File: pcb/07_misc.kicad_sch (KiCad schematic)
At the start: 0 parts

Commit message: Added four mounting holes connected to chassis with decoupling to gnd and one single connection from chassis to gnd
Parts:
- added C701, C702, C703, C704: 1nF 1kV, FluxNode-FOC:C_0603_1608_DensityHigh, symbol Device:C
- added H701, H702, H703, H704: MountingHole_Pad, MountingHole:MountingHole_3.2mm_M3_Pad_Via, symbol Mechanical:MountingHole_Pad
- added R701, R702, R703, R704: 0R, FluxNode-FOC:R_0603_1608_DensityHigh, symbol Device:R
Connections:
- new net CHASSIS: C701.1, C702.1, C703.1, C704.1, H701.1, H702.1, H703.1, H704.1, R701.1, R702.1, R703.1, R704.1
- new net GND: C701.2, C702.2, C703.2, C704.2, R701.2, R702.2, R703.2, R704.2

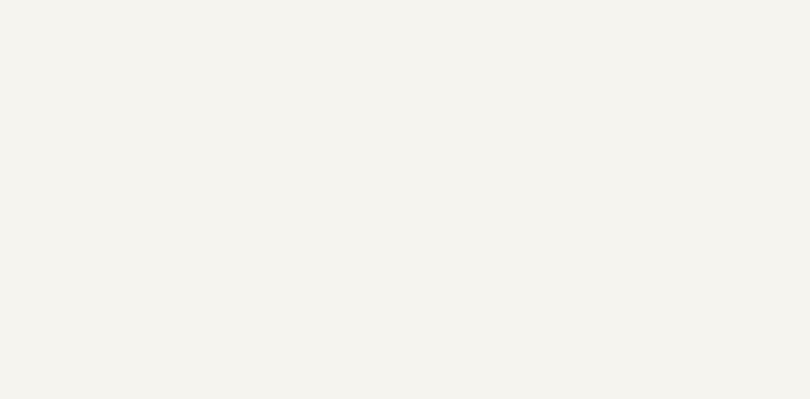
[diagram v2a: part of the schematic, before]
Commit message: Added fiducials for the top and bottom PCB side
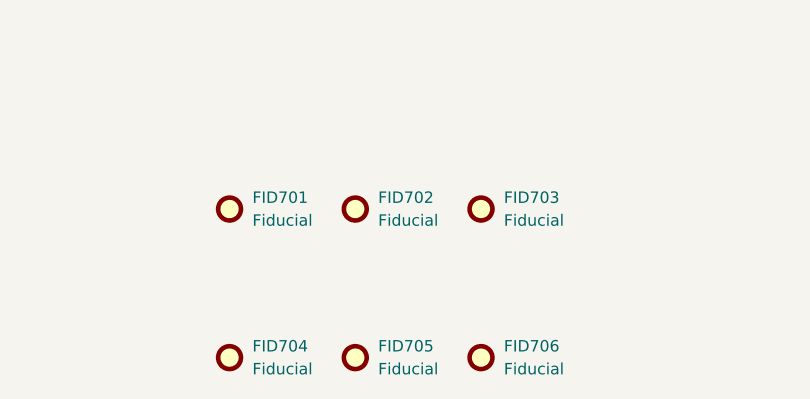
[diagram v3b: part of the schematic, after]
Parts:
- added FID701, FID702, FID703, FID704, FID705, FID706: Fiducial, Fiducial:Fiducial_1mm_Mask2mm, symbol Mechanical:Fiducial

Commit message: Unified all different LCSC part numbers of the same exact components to just one variant
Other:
- company: (none) -> PhiMai
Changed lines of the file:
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@@
 	(generator_version "10.0")
 	(paper "A4")
+	(title_block
+		(date "2026-06-07")
+		(rev "0.1.0")
+		(company "PhiMai")
+	)
 	(junction
 		(at 101.6 46.99)
